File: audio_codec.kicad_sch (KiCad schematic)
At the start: 38 parts, among them J2 AudioOutput, J3 AudioInput, J4 Headphones, U2 WM8731SEDS, U5 TPA6110A2DGN

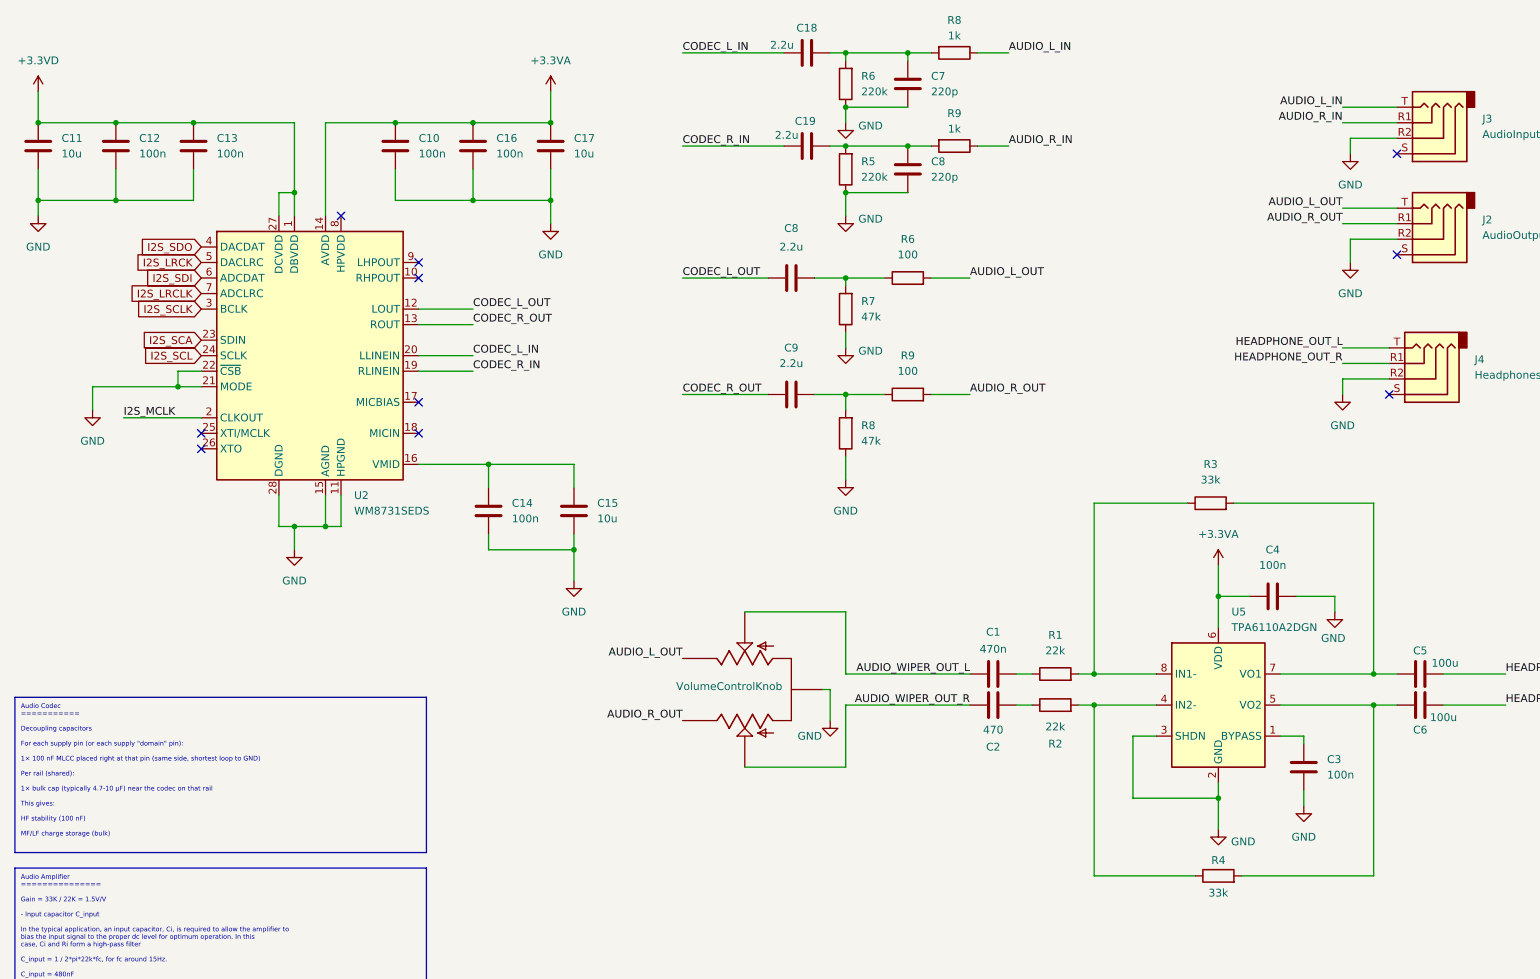
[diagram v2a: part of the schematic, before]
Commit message: adde boot switch
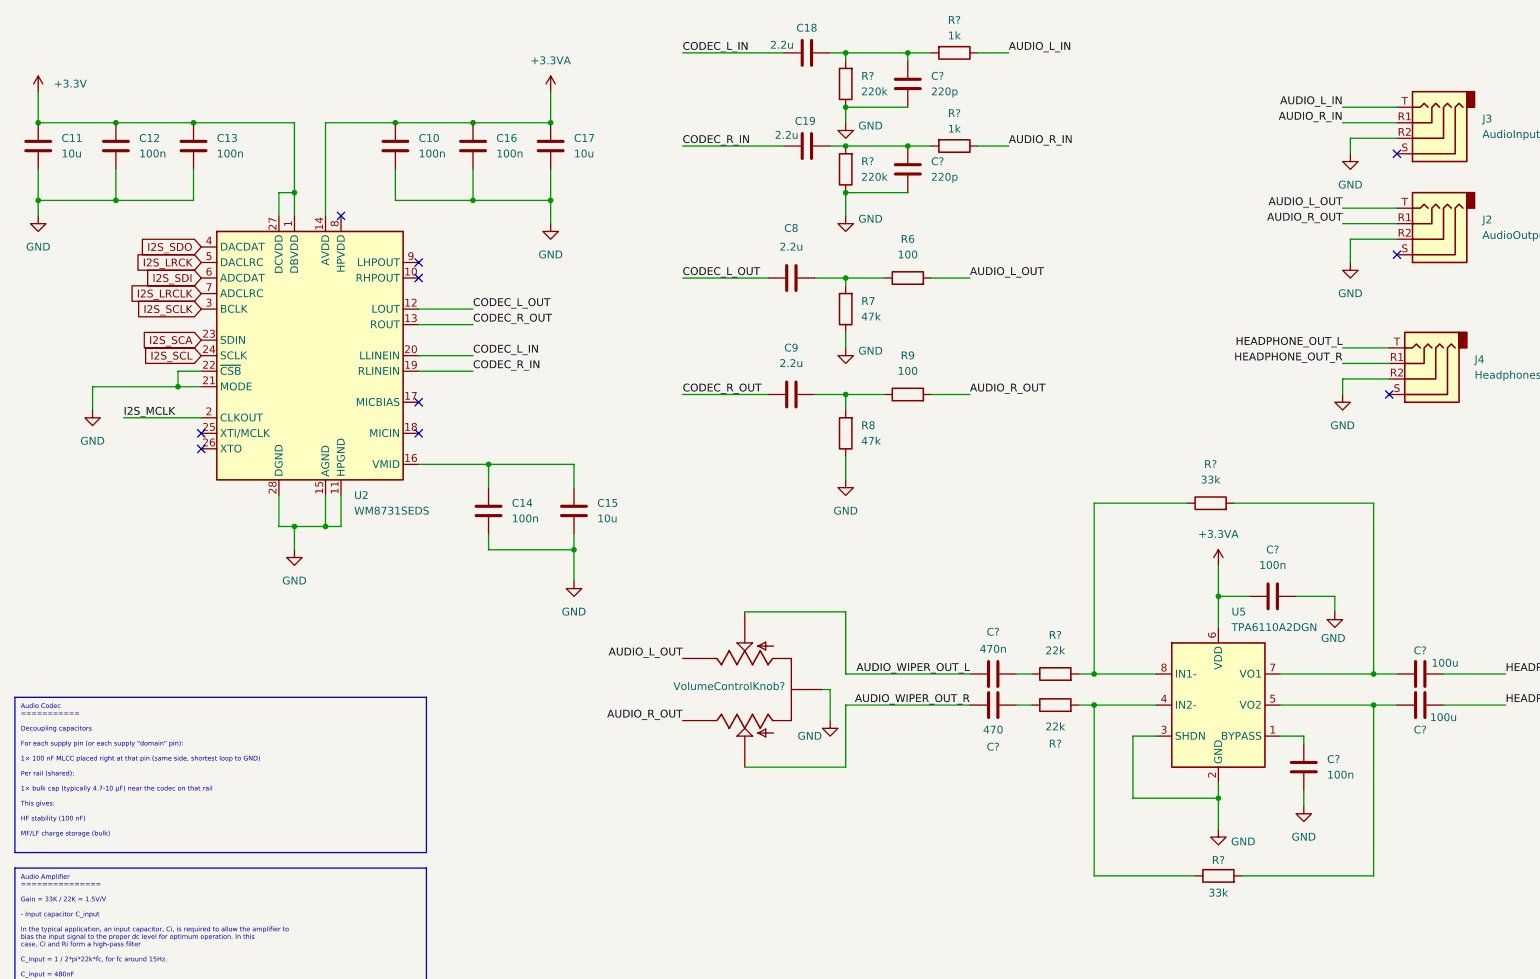
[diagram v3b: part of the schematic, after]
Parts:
- renumbered C2 to C?, C3 to C?, C4 to C?, C1 to C?, C8 to C?, C5 to C?, C6 to C?, C7 to C?, R4 to R?, R6 to R?, R2 to R?, R8 to R?, R1 to R?, R3 to R?, R5 to R?, R9 to R?, VolumeControlKnob to VolumeControlKnob?
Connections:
- net +3.3VD renamed +3.3V
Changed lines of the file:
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@@
 		(dnp no)
 		(fields_autoplaced yes)
-		(property "Reference" "#PWR04"
+		(property "Reference" "#PWR?"
 			(at 234.95 81.28 0)
 			(effects
@@
 		(on_board yes)
 		(dnp no)
-		(property "Reference" "#PWR01"
+		(property "Reference" "#PWR?"
 			(at 233.68 116.84 0)
 			(effects
@@
 		(on_board yes)
 		(dnp no)
-		(property "Reference" "R4"
+		(property "Reference" "R?"
 			(at 214.63 151.13 90)
 			(effects
@@
 		(on_board yes)
 		(dnp no)
-		(property "Reference" "C2"
+		(property "Reference" "C?"
 			(at 177.8 132.588 90)
 			(effects
@@
 		(dnp no)
 		(fields_autoplaced yes)
-		(property "Reference" "R6"
+		(property "Reference" "R?"
 			(at 156.21 22.8599 0)
 			(effects
@@
 		(on_board yes)
 		(dnp no)
-		(property "Reference" "R2"
+		(property "Reference" "R?"
 			(at 187.96 132.08 90)
 			(effects
@@
 		(dnp no)
 		(fields_autoplaced yes)
-		(property "Reference" "#PWR?"
+		(property "Reference" "#PWR020"
 			(at 236.22 41.91 0)
 			(effects
@@
 		(dnp no)
 		(fields_autoplaced yes)
-		(property "Reference" "R?"
+		(property "Reference" "R6"
 			(at 163.83 49.53 90)
 			(effects
@@
 		(dnp no)
 		(fields_autoplaced yes)
-		(property "Reference" "J?"
+		(property "Reference" "J3"
 			(at 257.81 29.8449 0)
 			(effects
@@
 		(dnp no)
 		(fields_autoplaced yes)
-		(property "Reference" "#PWR?"
+		(property "Reference" "#PWR017"
 			(at 105.41 29.21 0)
 			(effects
@@
 		(dnp no)
 		(fields_autoplaced yes)
-		(property "Reference" "#PWR?"
+		(property "Reference" "#PWR018"
 			(at 153.67 95.25 0)
 			(effects
@@
 		(dnp no)
 		(fields_autoplaced yes)
-		(property "Reference" "C?"
+		(property "Reference" "C17"
 			(at 109.22 33.0199 0)
 			(effects
@@
 		(dnp no)
 		(fields_autoplaced yes)
-		(property "Reference" "J?"
+		(property "Reference" "J2"
 			(at 257.81 46.3549 0)
 			(effects
@@
 		(on_board yes)
 		(dnp no)
-		(property "Reference" "#PWR?"
+		(property "Reference" "#PWR021"
 			(at 214.63 152.4 0)
 			(effects
@@
 		(dnp no)
 		(fields_autoplaced yes)
-		(property "Reference" "C?"
+		(property "Reference" "C14"
 			(at 99.06 92.7099 0)
 			(effects
@@
 		(on_board yes)
 		(dnp no)
-		(property "Reference" "#PWR?"
+		(property "Reference" "#PWR09"
 			(at 153.67 73.66 0)
 			(effects
@@
 		(dnp no)
 		(fields_autoplaced yes)
-		(property "Reference" "C3"
+		(property "Reference" "C?"
 			(at 232.41 134.6199 0)
 			(effects
@@
 		(dnp no)
 		(fields_autoplaced yes)
-		(property "Reference" "C4"
+		(property "Reference" "C?"
 			(at 223.52 100.33 90)
 			(effects
@@
 		(dnp no)
 		(fields_autoplaced yes)
-		(property "Reference" "U?"
+		(property "Reference" "U2"
 			(at 73.2633 91.44 0)
 			(effects
@@
 		(dnp no)
 		(fields_autoplaced yes)
-		(property "Reference" "C?"
+		(property "Reference" "C15"
 			(at 113.03 92.7099 0)
 			(effects
@@
 		(dnp no)
 		(fields_autoplaced yes)
-		(property "Reference" "R?"
+		(property "Reference" "R7"
 			(at 156.21 59.6899 0)
 			(effects
@@
 		(dnp no)
 		(fields_autoplaced yes)
-		(property "Reference" "#PWR?"
+		(property "Reference" "#PWR015"
 			(at 30.48 83.82 0)
 			(effects
@@
 		(on_board yes)
 		(dnp no)
-		(property "Reference" "C?"
+		(property "Reference" "C18"
 			(at 147.32 14.986 90)
 			(effects
@@
 		(on_board yes)
 		(dnp no)
-		(property "Reference" "C?"
+		(property "Reference" "C19"
 			(at 147.066 30.226 90)
 			(effects
@@
 		(on_board yes)
 		(dnp no)
-		(property "Reference" "VolumeControlKnob"
+		(property "Reference" "VolumeControlKnob?"
 			(at 134.62 122.682 90)
 			(effects
@@
 		(dnp no)
 		(fields_autoplaced yes)
-		(property "Reference" "C?"
+		(property "Reference" "C12"
 			(at 38.1 33.0199 0)
 			(effects
@@
 		(on_board yes)
 		(dnp no)
-		(property "Reference" "C1"
+		(property "Reference" "C?"
 			(at 177.8 113.792 90)
 			(effects
@@
 		(dnp no)
 		(fields_autoplaced yes)
-		(property "Reference" "#PWR?"
+		(property "Reference" "#PWR07"
 			(at 105.41 53.34 0)
 			(effects
@@
 		(dnp no)
 		(fields_autoplaced yes)
-		(property "Reference" "C?"
+		(property "Reference" "C9"
 			(at 144.78 67.31 90)
 			(effects
@@
 		(dnp no)
 		(fields_autoplaced yes)
-		(property "Reference" "#PWR?"
+		(property "Reference" "#PWR019"
 			(at 236.22 59.69 0)
 			(effects
@@
 		(on_board yes)
 		(dnp no)
-		(property "Reference" "#PWR?"
+		(property "Reference" "#PWR022"
 			(at 151.13 134.62 0)
 			(effects
@@
 		(on_board yes)
 		(dnp no)
-		(property "Reference" "R8"
+		(property "Reference" "R?"
 			(at 171.45 13.716 90)
 			(effects
@@
 		(dnp no)
 		(fields_autoplaced yes)
-		(property "Reference" "C?"
+		(property "Reference" "C13"
 			(at 50.8 33.0199 0)
 			(effects
@@
 		(dnp no)
 		(fields_autoplaced yes)
-		(property "Reference" "R?"
+		(property "Reference" "R9"
 			(at 163.83 68.58 90)
 			(effects
@@
 		(dnp no)
 		(fields_autoplaced yes)
-		(property "Reference" "R1"
+		(property "Reference" "R?"
 			(at 187.96 114.3 90)
 			(effects
@@
 		(on_board yes)
 		(dnp no)
-		(property "Reference" "C?"
+		(property "Reference" "C8"
 			(at 144.78 47.752 90)
 			(effects
@@
 		(dnp no)
 		(fields_autoplaced yes)
-		(property "Reference" "#PWR?"
+		(property "Reference" "#PWR016"
 			(at 109.22 111.76 0)
 			(effects
@@
 		(dnp no)
 		(fields_autoplaced yes)
-		(property "Reference" "J?"
+		(property "Reference" "J4"
 			(at 256.54 69.2149 0)
 			(effects
@@
 		(dnp no)
 		(fields_autoplaced yes)
-		(property "Reference" "R3"
+		(property "Reference" "R?"
 			(at 213.36 86.36 90)
 			(effects
@@
 		(dnp no)
 		(fields_autoplaced yes)
-		(property "Reference" "#PWR03"
+		(property "Reference" "#PWR?"
 			(at 228.6 148.59 0)
 			(effects
@@
 		(dnp no)
 		(fields_autoplaced yes)
-		(property "Reference" "R?"
+		(property "Reference" "R8"
 			(at 156.21 80.0099 0)
 			(effects
@@
 		(on_board yes)
 		(dnp no)
-		(property "Reference" "#PWR?"
+		(property "Reference" "#PWR01"
 			(at 63.5 106.68 0)
 			(effects
@@
 		(dnp no)
 		(fields_autoplaced yes)
-		(property "Reference" "#PWR?"
+		(property "Reference" "#PWR014"
 			(at 21.59 52.07 0)
 			(effects
@@
 		(dnp no)
 		(fields_autoplaced yes)
-		(property "Reference" "C?"
+		(property "Reference" "C10"
 			(at 83.82 33.0199 0)
 			(effects
@@
 		(on_board yes)
 		(dnp no)
-		(property "Reference" "#PWR05"
+		(property "Reference" "#PWR?"
 			(at 153.67 52.07 0)
 			(effects
@@
 		(dnp no)
 		(fields_autoplaced yes)
-		(property "Reference" "C8"
+		(property "Reference" "C?"
 			(at 167.64 36.8299 0)
 			(effects
@@
 		(on_board yes)
 		(dnp no)
-		(property "Reference" "#PWR06"
+		(property "Reference" "#PWR?"
 			(at 153.67 36.83 0)
 			(effects
@@
 		(dnp no)
 		(fields_autoplaced yes)
-		(property "Reference" "#PWR02"
+		(property "Reference" "#PWR?"
 			(at 214.63 106.68 0)
 			(effects
@@
 		(on_board yes)
 		(dnp no)
-		(property "Reference" "C5"
+		(property "Reference" "C?"
 			(at 247.65 116.84 90)
 			(effects
@@
 		(dnp no)
 		(fields_autoplaced yes)
-		(property "Reference" "C?"
+		(property "Reference" "C11"
 			(at 25.4 33.0199 0)
 			(effects
@@
 		(dnp no)
 		(fields_autoplaced yes)
-		(property "Reference" "R5"
+		(property "Reference" "R?"
 			(at 156.21 36.8299 0)
 			(effects
@@
 		(on_board yes)
 		(dnp no)
-		(property "Reference" "C6"
+		(property "Reference" "C?"
 			(at 247.65 129.794 90)
 			(effects
@@
 		(dnp no)
 		(fields_autoplaced yes)
-		(property "Reference" "C?"
+		(property "Reference" "C16"
 			(at 96.52 33.0199 0)
 			(effects
@@
 		(dnp no)
 		(fields_autoplaced yes)
-		(property "Reference" "#PWR?"
+		(property "Reference" "#PWR013"
 			(at 21.59 29.21 0)
 			(effects
@@
 			)
 		)
-		(property "Value" "+3.3VD"
-			(at 21.59 20.32 0)
+		(property "Value" "+3.3V"
+			(at 24.13 24.1299 0)
 			(effects
 				(font
 					(size 1.27 1.27)
 				)
+				(justify left)
 			)
 		)
@@
 		(dnp no)
 		(fields_autoplaced yes)
-		(property "Reference" "C7"
+		(property "Reference" "C?"
 			(at 167.64 22.8599 0)
 			(effects
@@
 		(on_board yes)
 		(dnp no)
-		(property "Reference" "R9"
+		(property "Reference" "R?"
 			(at 171.45 28.956 90)
 			(effects
@@
 		(dnp no)
 		(fields_autoplaced yes)
-		(property "Reference" "U?"
+		(property "Reference" "U5"
 			(at 216.7733 110.49 0)
 			(effects

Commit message: First pins assingments
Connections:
- net I2S_LRCLK is gone; now on net I2S_WS: U2.7 (ADCLRC)
- net IS2_MCLK: now reaches U2.25 (XTI/MCLK)
- net I2S_LRCK renamed I2S_WS
- net I2S_MCLK: no longer names the net of U2.2 (CLKOUT)
- net I2S_SCLK renamed I2S_CK
- net I2S_SDO renamed I2S_SD
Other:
- moved on the sheet: C18, C19, C8, C9, C?, R6, R7, R8, R9, R?, U5, VolumeControlKnob?

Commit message: MCU connected
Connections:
- net +3.3V renamed +3V3
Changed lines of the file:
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@@
 			)
 		)
-		(property "Value" "+3.3V"
+		(property "Value" "+3V3"
 			(at 24.13 24.1299 0)
 			(effects

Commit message: adding anotations
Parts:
- gave numbers to parts that had none: 17
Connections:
- net IS2_MCLK renamed IS2_MCk
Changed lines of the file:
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@@
 		)
 	)
-	(global_label "IS2_MCLK"
+	(global_label "IS2_MCk"
 		(shape input)
 		(at 45.72 81.28 180)
@@
 		)
 		(property "Intersheetrefs" "${INTERSHEET_REFS}"
-			(at 33.7239 81.28 0)
+			(at 34.9939 81.28 0)
 			(effects
 				(font
@@
 		(dnp no)
 		(fields_autoplaced yes)
-		(property "Reference" "#PWR?"
+		(property "Reference" "#PWR0116"
 			(at 234.95 81.28 0)
 			(effects
@@
 			(project "GalernaDsp"
 				(path "/a77f8f1b-3e6d-40f9-a36e-54a20299e9bc/c8eca522-3096-4cb1-b457-c66eaba9f73c"
-					(reference "#PWR?")
+					(reference "#PWR0116")
 					(unit 1)
 				)
@@
 		(on_board yes)
 		(dnp no)
-		(property "Reference" "#PWR?"
+		(property "Reference" "#PWR0119"
 			(at 231.14 121.92 0)
 			(effects
@@
 			(project "GalernaDsp"
 				(path "/a77f8f1b-3e6d-40f9-a36e-54a20299e9bc/c8eca522-3096-4cb1-b457-c66eaba9f73c"
-					(reference "#PWR?")
+					(reference "#PWR0119")
 					(unit 1)
 				)
@@
 		(on_board yes)
 		(dnp no)
-		(property "Reference" "R?"
+		(property "Reference" "R31"
 			(at 212.09 156.21 90)
 			(effects
@@
 			(project "GalernaDsp"
 				(path "/a77f8f1b-3e6d-40f9-a36e-54a20299e9bc/c8eca522-3096-4cb1-b457-c66eaba9f73c"
-					(reference "R?")
+					(reference "R31")
 					(unit 1)
 				)
@@
 		(on_board yes)
 		(dnp no)
-		(property "Reference" "C?"
+		(property "Reference" "C45"
 			(at 175.26 137.668 90)
 			(effects
@@
 			(project "GalernaDsp"
 				(path "/a77f8f1b-3e6d-40f9-a36e-54a20299e9bc/c8eca522-3096-4cb1-b457-c66eaba9f73c"
-					(reference "C?")
+					(reference "C45")
 					(unit 1)
 				)
@@
 		(dnp no)
 		(fields_autoplaced yes)
-		(property "Reference" "R?"
+		(property "Reference" "R24"
 			(at 162.56 31.7499 0)
 			(effects
@@
 			(project "GalernaDsp"
 				(path "/a77f8f1b-3e6d-40f9-a36e-54a20299e9bc/c8eca522-3096-4cb1-b457-c66eaba9f73c"
-					(reference "R?")
+					(reference "R24")
 					(unit 1)
 				)
@@
 		(on_board yes)
 		(dnp no)
-		(property "Reference" "R?"
+		(property "Reference" "R29"
 			(at 185.42 137.16 90)
 			(effects
@@
 			(project "GalernaDsp"
 				(path "/a77f8f1b-3e6d-40f9-a36e-54a20299e9bc/c8eca522-3096-4cb1-b457-c66eaba9f73c"
-					(reference "R?")
+					(reference "R29")
 					(unit 1)
 				)
@@
 		(dnp no)
 		(fields_autoplaced yes)
-		(property "Reference" "C?"
+		(property "Reference" "C47"
 			(at 229.87 139.6999 0)
 			(effects
@@
 			(project "GalernaDsp"
 				(path "/a77f8f1b-3e6d-40f9-a36e-54a20299e9bc/c8eca522-3096-4cb1-b457-c66eaba9f73c"
-					(reference "C?")
+					(reference "C47")
 					(unit 1)
 				)
@@
 		(dnp no)
 		(fields_autoplaced yes)
-		(property "Reference" "C?"
+		(property "Reference" "C46"
 			(at 220.98 105.41 90)
 			(effects
@@
 			(project "GalernaDsp"
 				(path "/a77f8f1b-3e6d-40f9-a36e-54a20299e9bc/c8eca522-3096-4cb1-b457-c66eaba9f73c"
-					(reference "C?")
+					(reference "C46")
 					(unit 1)
 				)
@@
 		(on_board yes)
 		(dnp no)
-		(property "Reference" "VolumeControlKnob?"
+		(property "Reference" "VolumeControlKnob1"
 			(at 132.08 127.762 90)
 			(effects
@@
 			(project "GalernaDsp"
 				(path "/a77f8f1b-3e6d-40f9-a36e-54a20299e9bc/c8eca522-3096-4cb1-b457-c66eaba9f73c"
-					(reference "VolumeControlKnob?")
+					(reference "VolumeControlKnob1")
 					(unit 1)
 				)
@@
 		(on_board yes)
 		(dnp no)
-		(property "Reference" "C?"
+		(property "Reference" "C44"
 			(at 175.26 118.872 90)
 			(effects
@@
 			(project "GalernaDsp"
 				(path "/a77f8f1b-3e6d-40f9-a36e-54a20299e9bc/c8eca522-3096-4cb1-b457-c66eaba9f73c"
-					(reference "C?")
+					(reference "C44")
 					(unit 1)
 				)
@@
 		(on_board yes)
 		(dnp no)
-		(property "Reference" "R?"
+		(property "Reference" "R26"
 			(at 177.8 22.606 90)
 			(effects
@@
 			(project "GalernaDsp"
 				(path "/a77f8f1b-3e6d-40f9-a36e-54a20299e9bc/c8eca522-3096-4cb1-b457-c66eaba9f73c"
-					(reference "R?")
+					(reference "R26")
 					(unit 1)
 				)
@@
 		(dnp no)
 		(fields_autoplaced yes)
-		(property "Reference" "R?"
+		(property "Reference" "R28"
 			(at 185.42 119.38 90)
 			(effects
@@
 			(project "GalernaDsp"
 				(path "/a77f8f1b-3e6d-40f9-a36e-54a20299e9bc/c8eca522-3096-4cb1-b457-c66eaba9f73c"
-					(reference "R?")
+					(reference "R28")
 					(unit 1)
 				)
@@
 		(dnp no)
 		(fields_autoplaced yes)
-		(property "Reference" "R?"
+		(property "Reference" "R30"
 			(at 210.82 91.44 90)
 			(effects
@@
 			(project "GalernaDsp"
 				(path "/a77f8f1b-3e6d-40f9-a36e-54a20299e9bc/c8eca522-3096-4cb1-b457-c66eaba9f73c"
-					(reference "R?")
+					(reference "R30")
 					(unit 1)
 				)
@@
 		(dnp no)
 		(fields_autoplaced yes)
-		(property "Reference" "#PWR?"
+		(property "Reference" "#PWR0117"
 			(at 226.06 153.67 0)
 			(effects
@@
 			(project "GalernaDsp"
 				(path "/a77f8f1b-3e6d-40f9-a36e-54a20299e9bc/c8eca522-3096-4cb1-b457-c66eaba9f73c"
-					(reference "#PWR?")
+					(reference "#PWR0117")
 					(unit 1)
 				)
@@
 		(on_board yes)
 		(dnp no)
-		(property "Reference" "#PWR?"
+		(property "Reference" "#PWR0121"
 			(at 160.02 60.96 0)
 			(effects
@@
 			(project "GalernaDsp"
 				(path "/a77f8f1b-3e6d-40f9-a36e-54a20299e9bc/c8eca522-3096-4cb1-b457-c66eaba9f73c"
-					(reference "#PWR?")
+					(reference "#PWR0121")
 					(unit 1)
 				)
@@
 		(dnp no)
 		(fields_autoplaced yes)
-		(property "Reference" "C?"
+		(property "Reference" "C43"
 			(at 173.99 45.7199 0)
 			(effects
@@
 			(project "GalernaDsp"
 				(path "/a77f8f1b-3e6d-40f9-a36e-54a20299e9bc/c8eca522-3096-4cb1-b457-c66eaba9f73c"
-					(reference "C?")
+					(reference "C43")
 					(unit 1)
 				)
@@
 		(on_board yes)
 		(dnp no)
-		(property "Reference" "#PWR?"
+		(property "Reference" "#PWR0120"
 			(at 160.02 45.72 0)
 			(effects
@@
 			(project "GalernaDsp"
 				(path "/a77f8f1b-3e6d-40f9-a36e-54a20299e9bc/c8eca522-3096-4cb1-b457-c66eaba9f73c"
-					(reference "#PWR?")
+					(reference "#PWR0120")
 					(unit 1)
 				)
@@
 		(dnp no)
 		(fields_autoplaced yes)
-		(property "Reference" "#PWR?"
+		(property "Reference" "#PWR0118"
 			(at 212.09 111.76 0)
 			(effects
@@
 			(project "GalernaDsp"
 				(path "/a77f8f1b-3e6d-40f9-a36e-54a20299e9bc/c8eca522-3096-4cb1-b457-c66eaba9f73c"
-					(reference "#PWR?")
+					(reference "#PWR0118")
 					(unit 1)
 				)
@@
 		(on_board yes)
 		(dnp no)
-		(property "Reference" "C?"
+		(property "Reference" "C48"
 			(at 245.11 121.92 90)
 			(effects
@@
 			(project "GalernaDsp"
 				(path "/a77f8f1b-3e6d-40f9-a36e-54a20299e9bc/c8eca522-3096-4cb1-b457-c66eaba9f73c"
-					(reference "C?")
+					(reference "C48")
 					(unit 1)
 				)
@@
 		(dnp no)
 		(fields_autoplaced yes)
-		(property "Reference" "R?"
+		(property "Reference" "R25"
 			(at 162.56 45.7199 0)
 			(effects
@@
 			(project "GalernaDsp"
 				(path "/a77f8f1b-3e6d-40f9-a36e-54a20299e9bc/c8eca522-3096-4cb1-b457-c66eaba9f73c"
-					(reference "R?")
+					(reference "R25")
 					(unit 1)
 				)
@@
 		(on_board yes)
 		(dnp no)
-		(property "Reference" "C?"
+		(property "Reference" "C49"
 			(at 245.11 134.874 90)
 			(effects
@@
 			(project "GalernaDsp"
 				(path "/a77f8f1b-3e6d-40f9-a36e-54a20299e9bc/c8eca522-3096-4cb1-b457-c66eaba9f73c"
-					(reference "C?")
+					(reference "C49")
 					(unit 1)
 				)
@@
 		(dnp no)
 		(fields_autoplaced yes)
-		(property "Reference" "C?"
+		(property "Reference" "C42"
 			(at 173.99 31.7499 0)
 			(effects
@@
 			(project "GalernaDsp"
 				(path "/a77f8f1b-3e6d-40f9-a36e-54a20299e9bc/c8eca522-3096-4cb1-b457-c66eaba9f73c"
-					(reference "C?")
+					(reference "C42")
 					(unit 1)
 				)
@@
 		(on_board yes)
 		(dnp no)
-		(property "Reference" "R?"
+		(property "Reference" "R27"
 			(at 177.8 37.846 90)
 			(effects
@@
 			(project "GalernaDsp"
 				(path "/a77f8f1b-3e6d-40f9-a36e-54a20299e9bc/c8eca522-3096-4cb1-b457-c66eaba9f73c"
-					(reference "R?")
+					(reference "R27")
 					(unit 1)
 				)
